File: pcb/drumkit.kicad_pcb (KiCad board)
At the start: 2 copper layers, 22 parts, among them IC1 ULN2065B, J1 BATTERY, J2 Conn_01x04_Female, J3 CH1, J4 CH2, J5 CH3, SW1 BUTTON1, SW2 BUTTON2, SW3 BUTTON3, SW4 BUTTON4, SW5 POWER_SW, U1 Pico, U2 Mini360

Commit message: fix board
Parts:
- removed IC1: ULN2065B, Package_DIP:DIP-16_W7.62mm_LongPads
- removed J3: CH1, TerminalBlock:TerminalBlock_bornier-2_P5.08mm
- removed J4: CH2, TerminalBlock:TerminalBlock_bornier-2_P5.08mm
- removed J5: CH3, TerminalBlock:TerminalBlock_bornier-2_P5.08mm
- added U3: ~, chinese_modules:dc-dc module, F.Cu at (109.1, 45.8)
- added U4: ~, chinese_modules:xy-mos, F.Cu at (122.0, 19.3)
- added U5: ~, chinese_modules:dc-dc module, F.Cu at (147.8, 45.8)
- added U6: ~, chinese_modules:xy-mos, F.Cu at (160.8, 19.3)
- added U7: ~, chinese_modules:dc-dc module, F.Cu at (186.6, 45.8)
- added U8: ~, chinese_modules:xy-mos, F.Cu at (199.5, 19.3)
- U2: value Mini360 -> ~; footprint Mini360_step-down:Mini360_step-down -> chinese_modules:charger
- moved J1 140.0 mm to (200.0, 79.4)
- moved SW5 89.1 mm to (165.3, 66.7)
- moved U2 87.7 mm to (189.3, 66.1), turned to 180 degrees
- moved D1 68.5 mm to (133.3, 90.8)
- moved SW1 66.2 mm to (133.3, 107.0), turned to 90 degrees
- moved D2 62.8 mm to (152.4, 90.8)
- moved R1 62.2 mm to (142.9, 94.6)
- moved SW2 60.3 mm to (152.4, 107.0), turned to 90 degrees
- moved D3 57.7 mm to (172.1, 90.8)
- moved R2 56.7 mm to (161.9, 94.6)
- moved SW3 54.4 mm to (171.4, 107.0), turned to 90 degrees
- moved D4 51.8 mm to (190.5, 90.8)
- moved R3 50.9 mm to (181.0, 94.6)
- moved R4 49.9 mm to (200.0, 94.6)
- moved SW4 48.7 mm to (190.5, 107.0), turned to 90 degrees
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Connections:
- J2 pad 1: GND -> Net-(J2-Pin_1)
- S1 pad 1: Net-(U1-GPIO11) -> Net-(U1-GPIO16)
- SW1 pad 2: Net-(U1-GPIO5) -> Net-(U1-GPIO8)
- SW2 pad 2: Net-(U1-GPIO6) -> Net-(U1-GPIO9)
- SW3 pad 2: Net-(U1-GPIO7) -> Net-(U1-GPIO12)
- SW4 pad 2: Net-(U1-GPIO8) -> Net-(U1-GPIO14)
- U1 pad 10: Net-(U1-GPIO7) -> unconnected-(U1-GPIO7-Pad10)
- U1 pad 12: Net-(S1-CH_A) -> Net-(U1-GPIO9)
- U1 pad 13: unconnected-(U1-GND-Pad13) -> Net-(J2-Pin_1)
- U1 pad 14: Net-(S1-CH_B) -> Net-(D1-A)
- U1 pad 15: Net-(U1-GPIO11) -> Net-(D2-A)
- U1 pad 16: Net-(D1-A) -> Net-(U1-GPIO12)
- U1 pad 17: Net-(D2-A) -> Net-(D3-A)
- U1 pad 19: Net-(D3-A) -> Net-(U1-GPIO14)
- U1 pad 21: unconnected-(U1-GPIO16-Pad21) -> Net-(U1-GPIO16)
- U1 pad 22: unconnected-(U1-GPIO17-Pad22) -> Net-(S1-CH_A)
- U1 pad 23: unconnected-(U1-GND-Pad23) -> GND
- U1 pad 24: unconnected-(U1-GPIO18-Pad24) -> Net-(S1-CH_B)
- U1 pad 29: unconnected-(U1-GPIO22-Pad29) -> Net-(U1-GPIO22)
- U1 pad 31: unconnected-(U1-GPIO26_ADC0-Pad31) -> Net-(U1-GPIO26_ADC0)
- U1 pad 32: unconnected-(U1-GPIO27_ADC1-Pad32) -> Net-(U1-GPIO27_ADC1)
- U1 pad 39: unconnected-(U1-VSYS-Pad39) -> +BATT
- U1 pad 4: Net-(IC1-I3) -> unconnected-(U1-GPIO2-Pad4)
- U1 pad 5: Net-(IC1-I2) -> unconnected-(U1-GPIO3-Pad5)
- U1 pad 6: Net-(IC1-I1) -> unconnected-(U1-GPIO4-Pad6)
- U1 pad 7: Net-(U1-GPIO5) -> unconnected-(U1-GPIO5-Pad7)
- U1 pad 9: Net-(U1-GPIO6) -> unconnected-(U1-GPIO6-Pad9)
- U2 pad 1: GND -> unconnected-(U2-Vin+-Pad1)
- U2 pad 2: +BATT -> unconnected-(U2-Vin--Pad2)
- U2 pad 3: GND -> Net-(J1-Pin_1)
- U2 pad 4: +3V3 -> GND
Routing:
- net +BATT: track 118.8 -> 305.4 mm
- net Net-(IC1-I2): track 135.6 -> 0.00 mm
- net Net-(IC1-I1): track 130.6 -> 0.00 mm
- net Net-(IC1-I3): track 100.4 -> 0.00 mm
- net Net-(U1-GPIO7): track 97.7 -> 0.00 mm
- net Net-(U1-GPIO6): track 87.7 -> 0.00 mm
- net Net-(U1-GPIO8): track 118.3 -> 30.9 mm
- net Net-(U1-GPIO22): track 0.00 -> 72.4 mm
- net Net-(U1-GPIO14): track 0.00 -> 70.7 mm
- net Net-(U1-GPIO27_ADC1): track 0.00 -> 66.8 mm
- net Net-(U1-GPIO5): track 64.5 -> 0.00 mm
- net Net-(U1-GPIO12): track 0.00 -> 61.1 mm
- net Net-(J2-Pin_1): track 0.00 -> 54.8 mm
- net GND: track 403.1 -> 351.6 mm
- net Net-(U1-GPIO9): track 0.00 -> 47.0 mm
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
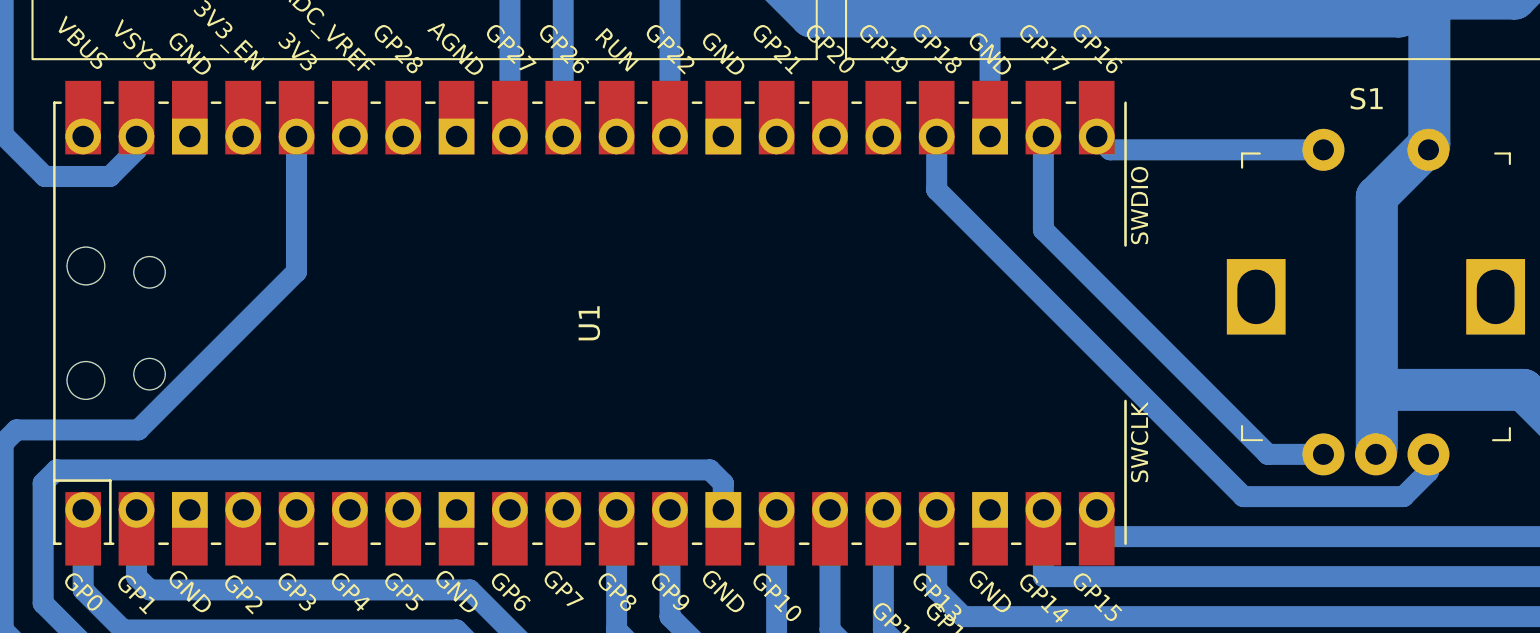
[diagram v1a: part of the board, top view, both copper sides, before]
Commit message: add voltage divider
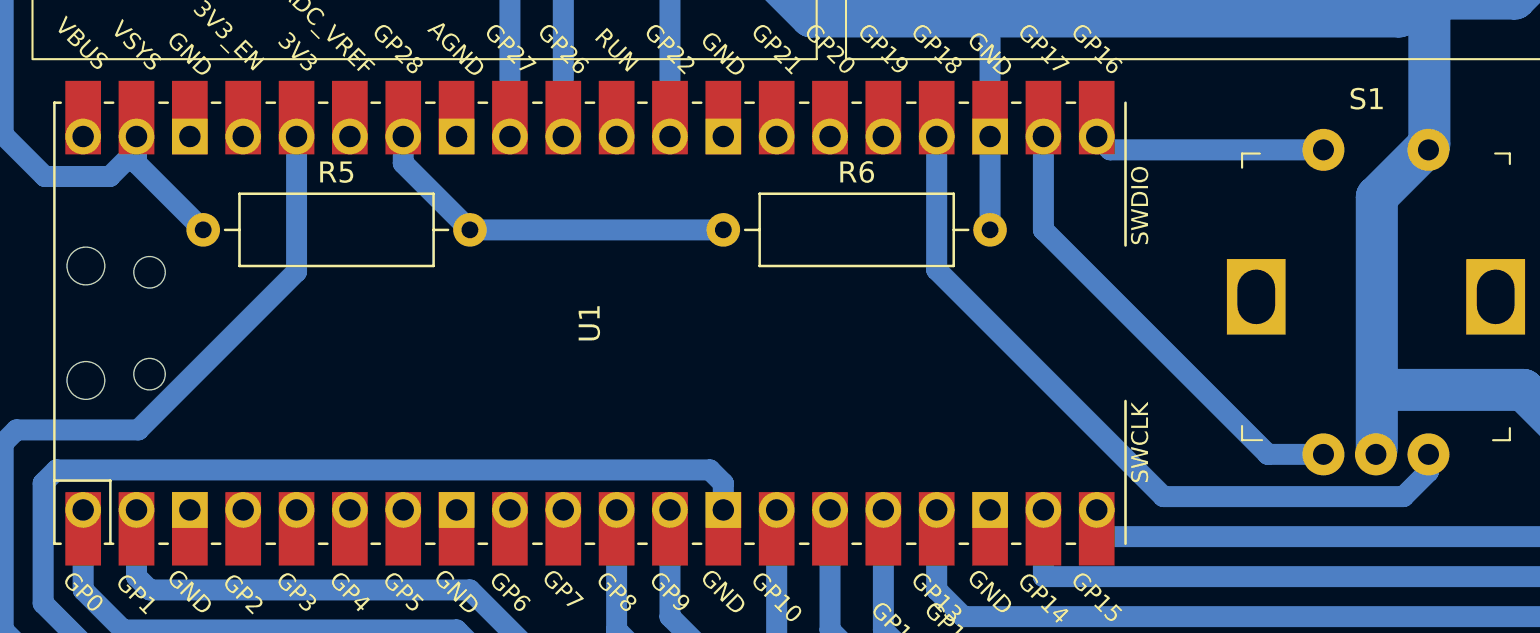
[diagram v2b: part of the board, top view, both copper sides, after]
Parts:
- added R5: R, Resistor_THT:R_Axial_DIN0309_L9.0mm_D3.2mm_P12.70mm_Horizontal, F.Cu at (95.9, 64.1)
- added R6: R, Resistor_THT:R_Axial_DIN0309_L9.0mm_D3.2mm_P12.70mm_Horizontal, F.Cu at (120.7, 64.1)
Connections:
- U1 pad 34: unconnected-(U1-GPIO28_ADC2-Pad34) -> Net-(U1-GPIO28_ADC2)
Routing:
- net Net-(U1-GPIO28_ADC2): track 0.00 -> 17.8 mm
- net +BATT: track 305.4 -> 311.1 mm
- net GND: track 351.6 -> 356.1 mm
- net Net-(S1-CH_B): track 33.3 -> 35.5 mm

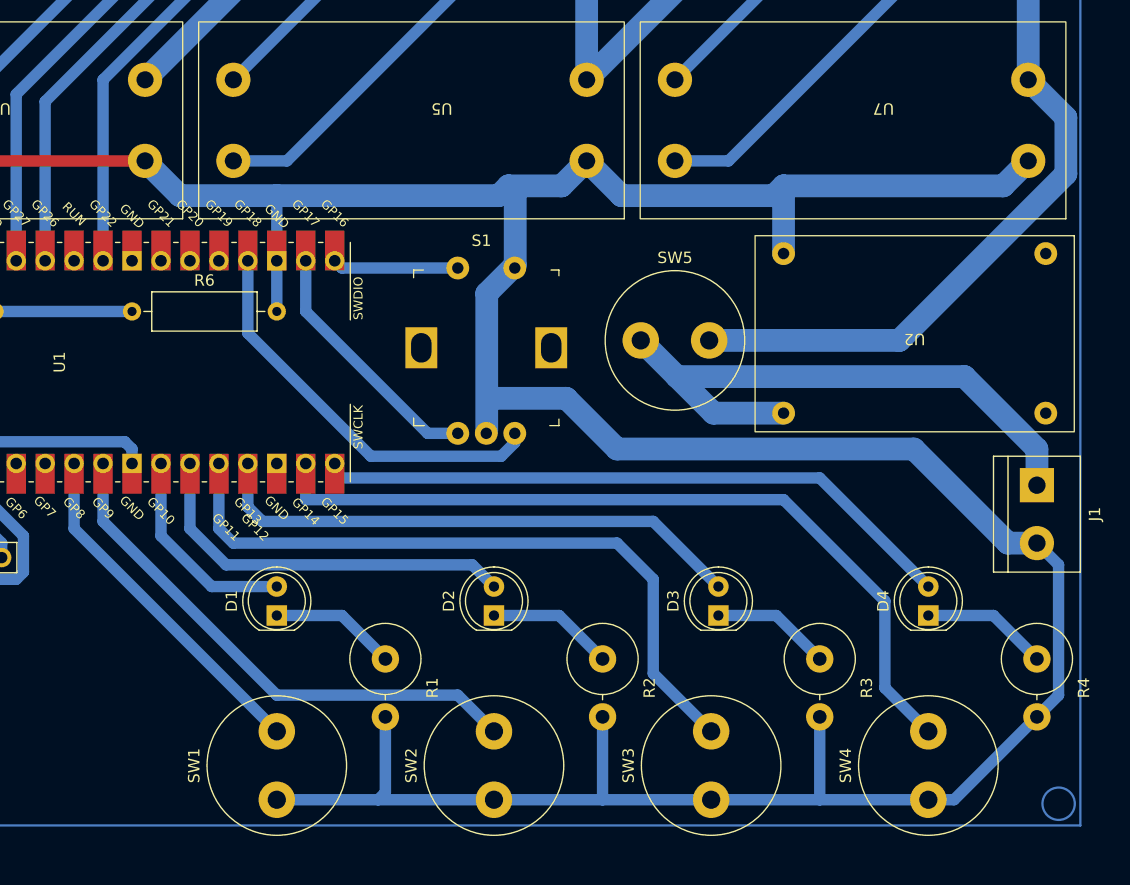
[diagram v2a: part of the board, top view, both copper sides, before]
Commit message: ipdate buttons footprints
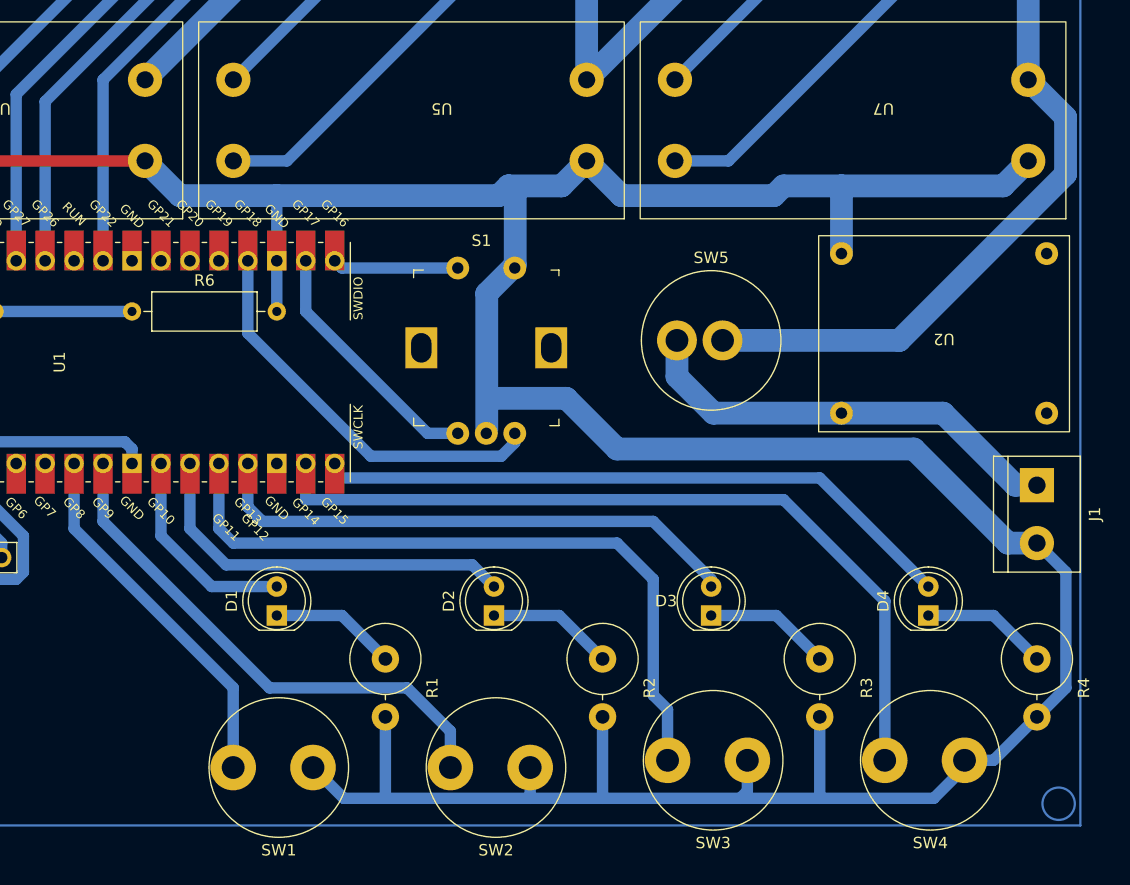
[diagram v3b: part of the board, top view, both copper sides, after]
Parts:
- moved SW3 4.70 mm to (174.6, 103.5), turned to 180 degrees
- moved SW4 4.70 mm to (193.7, 103.5), turned to 180 degrees
- moved SW1 4.25 mm to (136.5, 104.1), turned to 180 degrees
- moved SW2 4.25 mm to (155.6, 104.1), turned to 180 degrees
- moved SW5 3.17 mm to (168.4, 66.7)
- moved U2 2.58 mm to (191.9, 66.1)
- moved D3 0.64 mm to (171.4, 90.8)
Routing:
- net Net-(J1-Pin_1): track 52.5 -> 38.7 mm
- net GND: track 356.1 -> 360.0 mm
- net Net-(U1-GPIO14): track 70.7 -> 72.3 mm
- net Net-(U1-GPIO8): track 30.9 -> 32.5 mm
- net +BATT: track 311.1 -> 309.9 mm
- net Net-(U1-GPIO12): track 61.1 -> 62.1 mm
- net Net-(U1-GPIO9): track 47.0 -> 46.4 mm
- net Net-(D3-K): track 10.5 -> 11.1 mm

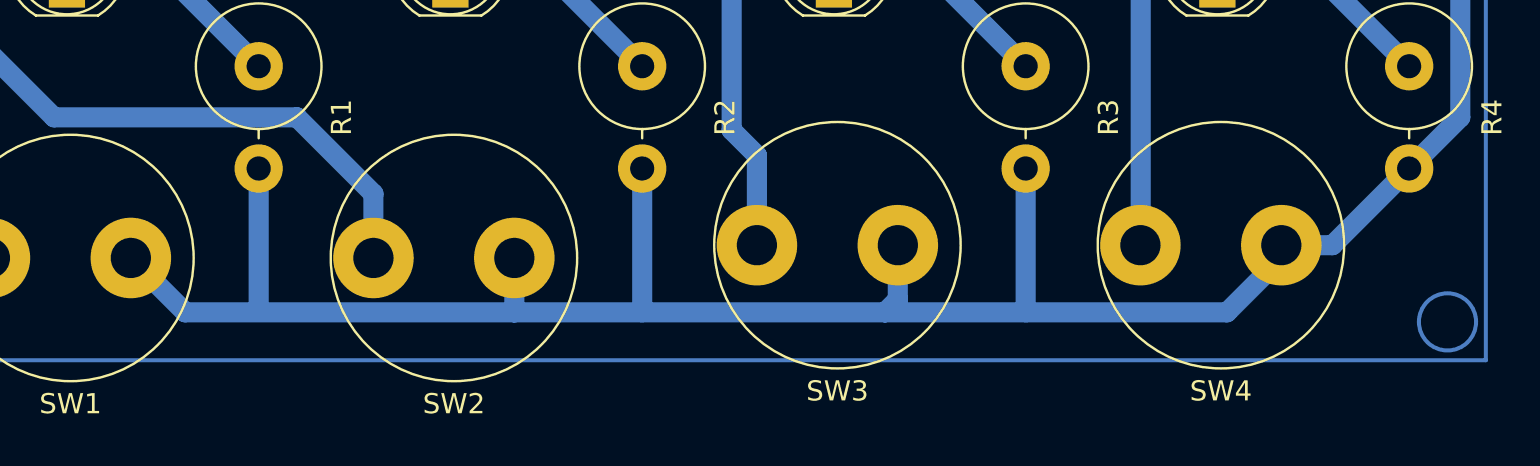
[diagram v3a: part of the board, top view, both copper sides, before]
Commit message: fix button placement
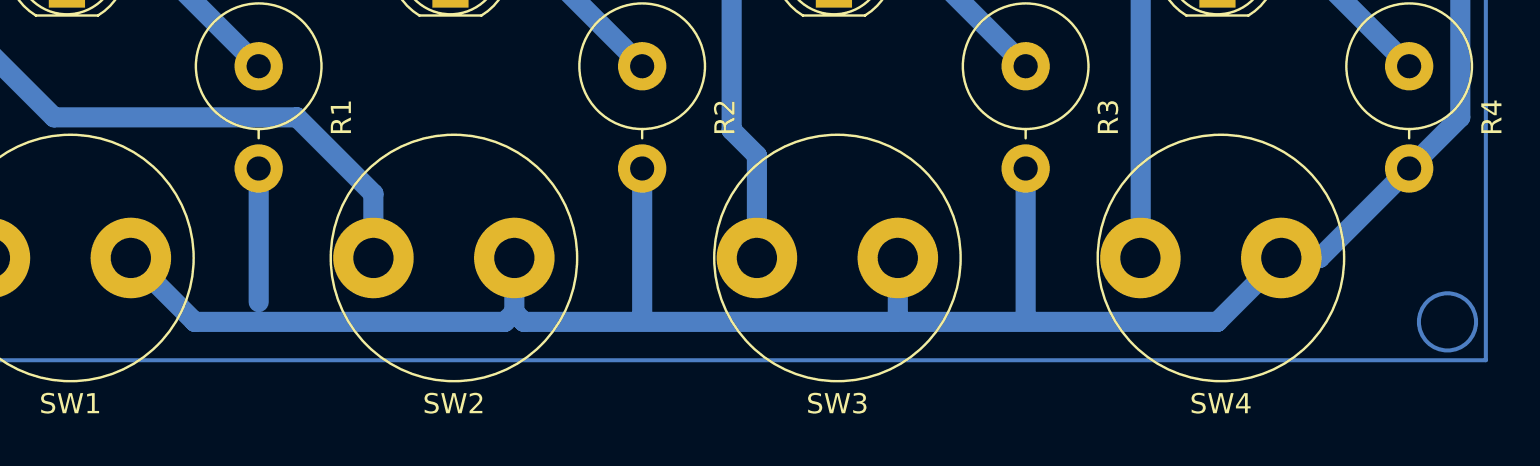
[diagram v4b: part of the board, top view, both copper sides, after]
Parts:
- moved SW3 0.64 mm to (174.6, 104.1)
- moved SW4 0.64 mm to (193.7, 104.1)
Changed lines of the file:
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@@
   )
   (footprint "Inductor_THT:L_Radial_D12.0mm_P6.00mm_MuRATA_1900R" (layer "F.Cu")
-    (at 174.625 103.505 180)
+    (at 174.625 104.14 180)
     (descr "Inductor, Radial series, Radial, pin pitch=6.00mm, , diameter=12.0mm, MuRATA, 1900R, http://www.murata-ps.com/data/magnetics/kmp_1900r.pdf")
     (tags "Inductor Radial series Radial pin pitch 6.00mm  diameter 12.0mm MuRATA 1900R")
@@
   )
   (footprint "Inductor_THT:L_Radial_D12.0mm_P6.00mm_MuRATA_1900R" (layer "F.Cu")
-    (at 193.675 103.505 180)
+    (at 193.675 104.14 180)
     (descr "Inductor, Radial series, Radial, pin pitch=6.00mm, , diameter=12.0mm, MuRATA, 1900R, http://www.murata-ps.com/data/magnetics/kmp_1900r.pdf")
     (tags "Inductor Radial series Radial pin pitch 6.00mm  diameter 12.0mm MuRATA 1900R")
@@
   (segment (start 163.195 76.2) (end 189.23 76.2) (width 2) (layer "B.Cu") (net 8))
   (segment (start 154.265 60.06) (end 151.765 62.56) (width 2) (layer "B.Cu") (net 8))
-  (segment (start 196.215 103.505) (end 200.025 99.695) (width 1) (layer "B.Cu") (net 8))
   (segment (start 133.35 64.135) (end 133.35 59.69) (width 1) (layer "B.Cu") (net 8))
   (segment (start 202.565 86.995) (end 202.565 97.155) (width 1) (layer "B.Cu") (net 8))
+  (segment (start 195.58 104.14) (end 200.025 99.695) (width 1) (layer "B.Cu") (net 8))
   (segment (start 154.265 60.06) (end 154.265 53.716877) (width 2) (layer "B.Cu") (net 8))
-  (segment (start 136.525 104.14) (end 139.225 106.84) (width 1) (layer "B.Cu") (net 8))
+  (segment (start 174.625 104.14) (end 174.625 107.155) (width 1) (layer "B.Cu") (net 8))
   (segment (start 176.946877 53.975) (end 177.8 53.121877) (width 2) (layer "B.Cu") (net 8))
   (segment (start 142.875 99.695) (end 142.875 106.33) (width 1) (layer "B.Cu") (net 8))
+  (segment (start 155.575 106.84) (end 156.05 107.315) (width 1) (layer "B.Cu") (net 8))
   (segment (start 160.528 50.927) (end 163.576 53.975) (width 2) (layer "B.Cu") (net 8))
-  (segment (start 193.675 103.505) (end 196.215 103.505) (width 1) (layer "B.Cu") (net 8))
-  (segment (start 190.975 106.84) (end 193.675 104.14) (width 1) (layer "B.Cu") (net 8))
   (segment (start 152.816877 53.975) (end 153.67 53.121877) (width 2) (layer "B.Cu") (net 8))
+  (segment (start 156.05 107.315) (end 174.465 107.315) (width 1) (layer "B.Cu") (net 8))
   (segment (start 153.67 53.121877) (end 158.333123 53.121877) (width 2) (layer "B.Cu") (net 8))
   (segment (start 158.75 71.755) (end 163.195 76.2) (width 2) (layer "B.Cu") (net 8))
@@
   (segment (start 155.575 104.14) (end 155.575 106.84) (width 1) (layer "B.Cu") (net 8))
   (segment (start 202.565 97.155) (end 200.025 99.695) (width 1) (layer "B.Cu") (net 8))
-  (segment (start 174.625 103.505) (end 174.625 106.205) (width 1) (layer "B.Cu") (net 8))
-  (segment (start 193.675 104.14) (end 193.675 103.505) (width 1) (layer "B.Cu") (net 8))
+  (segment (start 136.525 104.14) (end 139.7 107.315) (width 1) (layer "B.Cu") (net 8))
+  (segment (start 190.5 107.315) (end 193.675 104.14) (width 1) (layer "B.Cu") (net 8))
   (segment (start 151.725 74.825) (end 151.725 72.43) (width 1) (layer "B.Cu") (net 8))
   (segment (start 90.805 50.927) (end 88.195 48.317) (width 1) (layer "B.Cu") (net 8))
@@
   (segment (start 121.793 50.927) (end 124.841 53.975) (width 2) (layer "B.Cu") (net 8))
   (segment (start 200.025 84.455) (end 202.565 86.995) (width 1) (layer "B.Cu") (net 8))
-  (segment (start 174.625 106.205) (end 173.99 106.84) (width 1) (layer "B.Cu") (net 8))
   (segment (start 154.265 53.716877) (end 153.67 53.121877) (width 2) (layer "B.Cu") (net 8))
   (segment (start 151.725 72.43) (end 152.4 71.755) (width 1) (layer "B.Cu") (net 8))
@@
   (segment (start 161.925 99.695) (end 161.925 106.84) (width 1) (layer "B.Cu") (net 8))
   (segment (start 197.485 84.455) (end 200.025 84.455) (width 2) (layer "B.Cu") (net 8))
-  (segment (start 155.575 106.84) (end 173.99 106.84) (width 1) (layer "B.Cu") (net 8))
-  (segment (start 173.99 106.84) (end 190.975 106.84) (width 1) (layer "B.Cu") (net 8))
   (segment (start 88.195 48.317) (end 88.195 41.98) (width 1) (layer "B.Cu") (net 8))
+  (segment (start 174.625 107.155) (end 174.465 107.315) (width 1) (layer "B.Cu") (net 8))
   (segment (start 182.88 53.121877) (end 182.88 59.055) (width 2) (layer "B.Cu") (net 8))
-  (segment (start 139.225 106.84) (end 155.575 106.84) (width 1) (layer "B.Cu") (net 8))
   (segment (start 124.841 53.975) (end 133.35 53.975) (width 2) (layer "B.Cu") (net 8))
   (segment (start 152.4 71.755) (end 158.75 71.755) (width 2) (layer "B.Cu") (net 8))
   (segment (start 151.765 62.56) (end 151.765 74.56) (width 2) (layer "B.Cu") (net 8))
   (segment (start 182.88 53.121877) (end 197.068123 53.121877) (width 2) (layer "B.Cu") (net 8))
+  (segment (start 174.465 107.315) (end 190.5 107.315) (width 1) (layer "B.Cu") (net 8))
+  (segment (start 139.7 107.315) (end 155.1 107.315) (width 1) (layer "B.Cu") (net 8))
   (segment (start 197.068123 53.121877) (end 199.263 50.927) (width 2) (layer "B.Cu") (net 8))
+  (segment (start 155.1 107.315) (end 155.575 106.84) (width 1) (layer "B.Cu") (net 8))
   (segment (start 158.333123 53.121877) (end 160.528 50.927) (width 2) (layer "B.Cu") (net 8))
   (segment (start 163.576 53.975) (end 176.946877 53.975) (width 2) (layer "B.Cu") (net 8))
   (segment (start 97.155 33.02) (end 113.411 33.02) (width 1) (layer "B.Cu") (net 8))
   (segment (start 180.975 99.695) (end 180.975 106.84) (width 1) (layer "B.Cu") (net 8))
+  (segment (start 193.675 104.14) (end 195.58 104.14) (width 1) (layer "B.Cu") (net 8))
   (segment (start 146.58 74.825) (end 149.225 74.825) (width 1) (layer "B.Cu") (net 10))
   (segment (start 135.89 64.135) (end 146.58 74.825) (width 1) (layer "B.Cu") (net 10))
@@
   (segment (start 128.27 83.185) (end 128.27 77.47) (width 1) (layer "B.Cu") (net 58))
   (segment (start 163.195 84.455) (end 129.54 84.455) (width 1) (layer "B.Cu") (net 58))
+  (segment (start 186.69 89.535) (end 177.8 80.645) (width 1) (layer "B.Cu") (net 59))
+  (segment (start 186.675 104.14) (end 186.69 104.125) (width 1) (layer "B.Cu") (net 59))
   (segment (start 177.8 80.645) (end 135.89 80.645) (width 1) (layer "B.Cu") (net 59))
-  (segment (start 186.69 89.535) (end 177.8 80.645) (width 1) (layer "B.Cu") (net 59))
   (segment (start 186.69 104.125) (end 186.69 89.535) (width 1) (layer "B.Cu") (net 59))
-  (segment (start 186.675 104.14) (end 186.69 104.125) (width 1) (layer "B.Cu") (net 59))
   (segment (start 135.89 80.645) (end 135.89 77.47) (width 1) (layer "B.Cu") (net 59))
   (segment (start 118.11 82.55) (end 132.715 97.155) (width 1) (layer "B.Cu") (net 61))
